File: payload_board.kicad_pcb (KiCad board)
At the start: 4 copper layers, 100 x 100 mm, 100 parts, among them IC1 RP2040_QFN56, IC2 AZ1117CH-3.3TRG1, J1 Cam_PicoLock, J12 5025700893, J12 FC Breakout, J15 SWC, J2 Cam_Conn, J3 Antenna_Conn, J4 usb jumper, J5 Display_Conn, J6 Breakout, J7 Molex_Micro_USB, J8 FC to EPS Connector, Q1 Q_PMOS_GSD, SW1 KMR2, SW2 KMR2, T13V TESTPOINTROUND1.5MMNO, T1V2 TESTPOINTROUND1.5MMNO, T3V3 TESTPOINTROUND1.5MMNO, U1 W25Q128JVPIQ TR, U2 MAX706RESA, U3 INA180A1, U4 INA180A1, U5 FAN5331SX, Y1 ABLS-12.000MHZ-B2-T

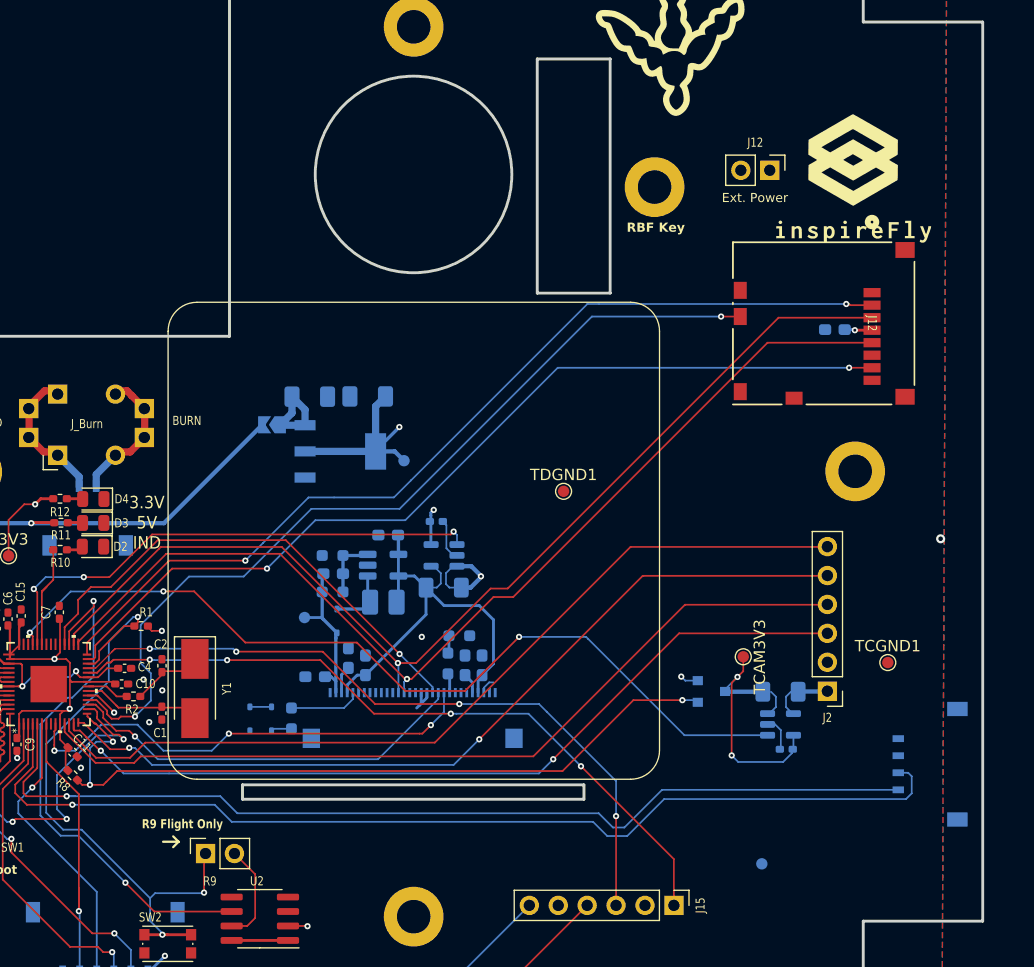
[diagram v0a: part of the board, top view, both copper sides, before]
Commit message: Moved some line appart
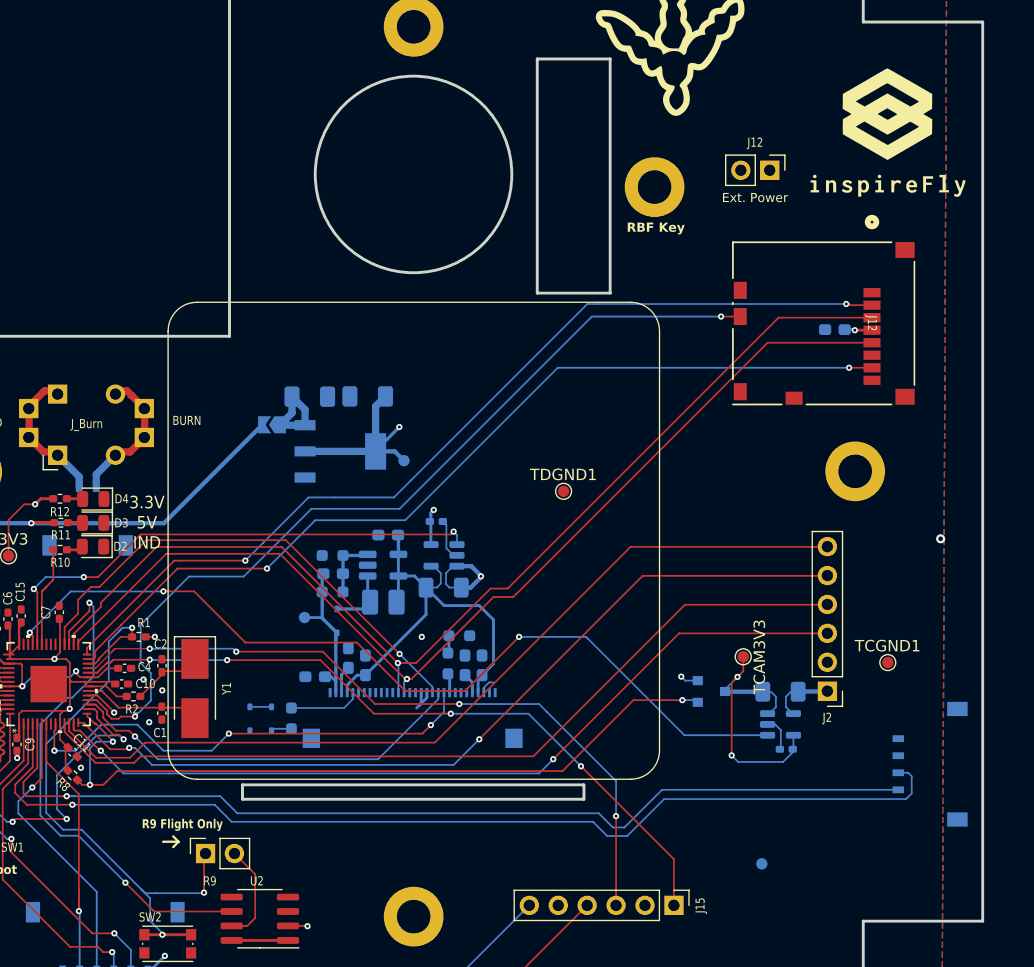
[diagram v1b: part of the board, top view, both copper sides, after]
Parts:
- moved G*** 5.04 mm to (104.6, 33.0)
- moved R1 0.97 mm to (38.8, 77.5)
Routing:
- net /~{RESET}: track 56.1 -> 55.1 mm
- net +3.3V: track 97.7 -> 97.0 mm

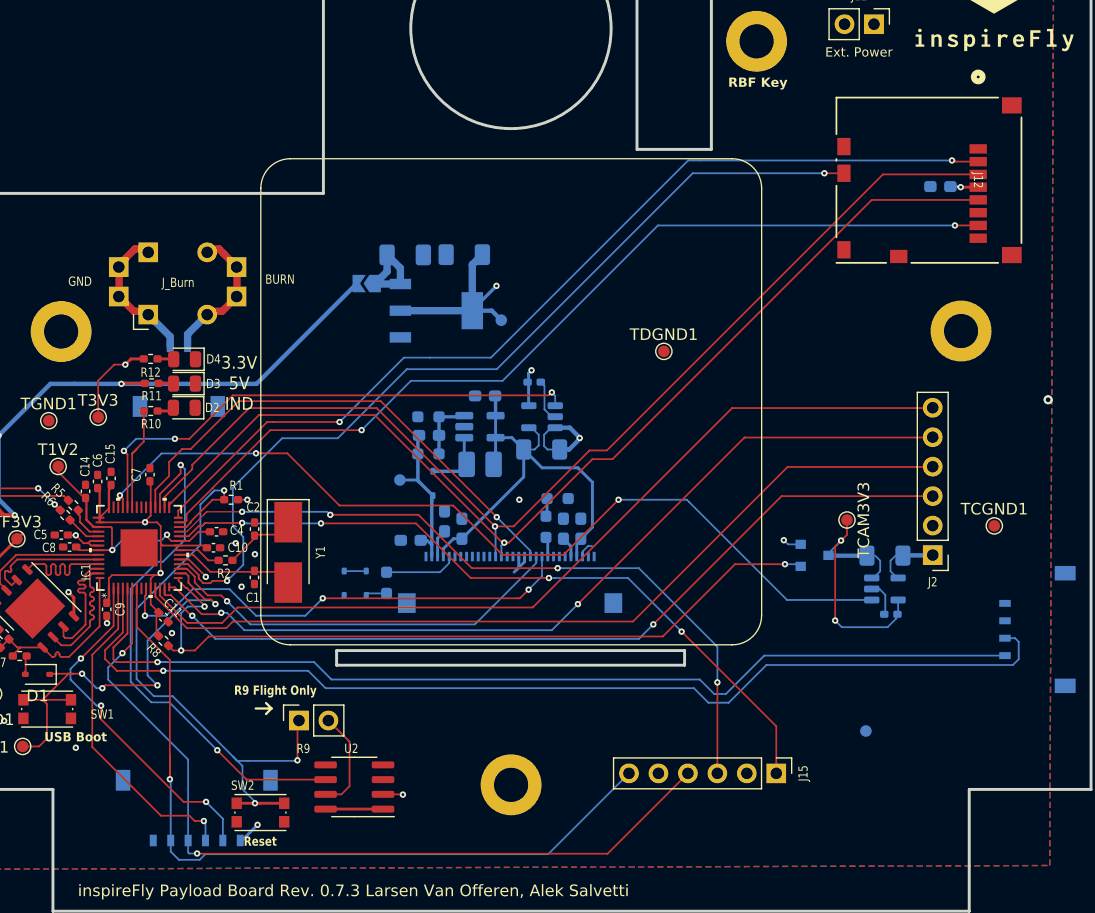
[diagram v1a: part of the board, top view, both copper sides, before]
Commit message: Fixed RP2040 connections and changed sd card
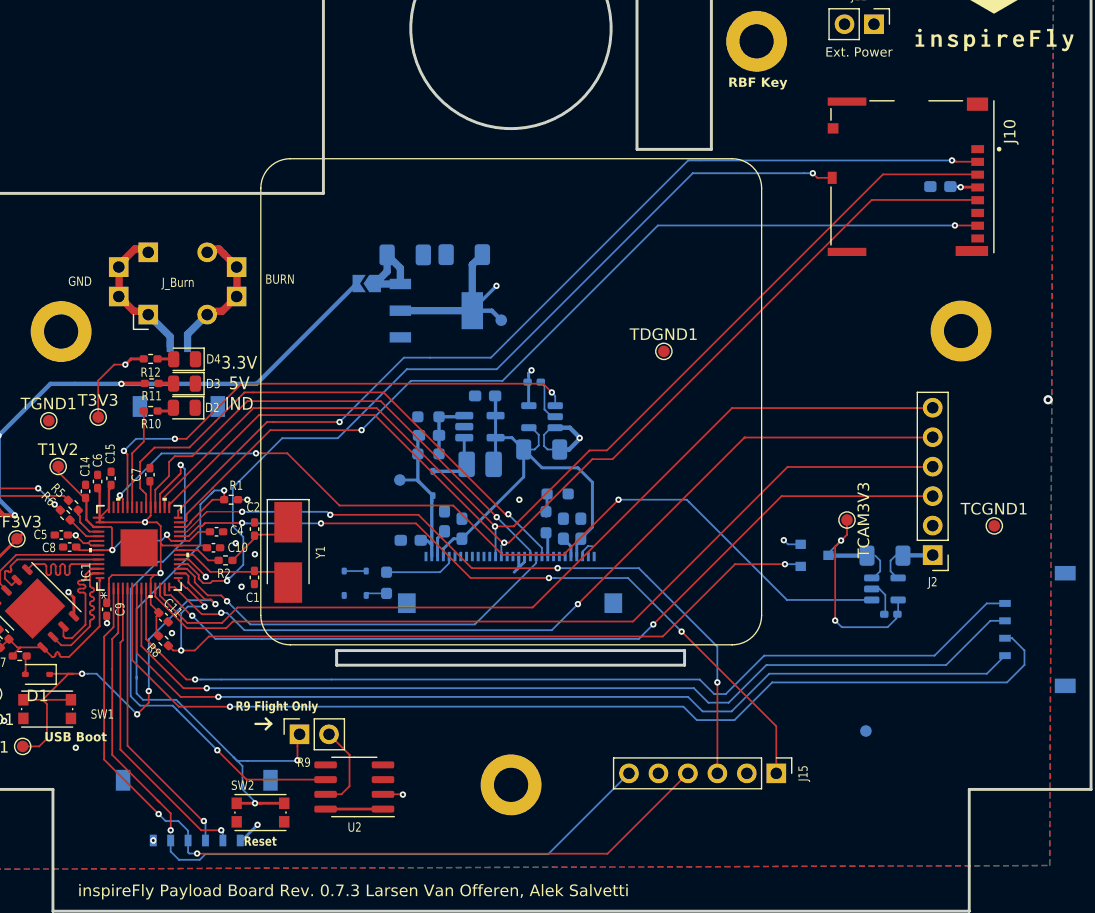
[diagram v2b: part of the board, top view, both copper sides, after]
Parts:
- removed the J12 at (99.0, 50.0)
- added J10: 503398-1892, PayloadBoard:MOLEX_503398-1892, F.Cu at (97.6, 49.7)
- moved R9 1.19 mm to (44.8, 97.7)
- moved R15 0.40 mm to (66.0, 79.4)
- moved R16 0.40 mm to (67.0, 77.0)
- turned C18 to 0 degrees
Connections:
- C18 pad 1: +3.3V -> GND
- C18 pad 2: GND -> +3.3V
- IC1 pad 2: Break_SDA -> UART1_TX
- IC1 pad 3: Break_SCL -> UART1_RX
- IC1 pad 34: unconnected-(IC1-GPIO22-Pad34) -> Disp_RST
- IC1 pad 4: I2C1_SDA -> Break_SDA
- IC1 pad 5: I2C1_SCL -> Break_SCL
- IC1 pad 6: UART1_TX -> I2C1_SDA
- IC1 pad 7: UART1_RX -> I2C1_SCL
- IC1 pad 8: unconnected-(IC1-GPIO6-Pad8) -> BURN_A
- IC1 pad 9: Disp_RST -> BURN_B
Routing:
- net BURN_A: track 0.00 -> 84.4 mm, vias 0 -> 1
- net BURN_B: track 0.00 -> 83.6 mm, vias 0 -> 1
- net Disp_RST: track 41.7 -> 47.6 mm, vias 3 -> 1
- net Break_SCL: track 28.7 -> 24.7 mm
- net Break_SDA: track 30.2 -> 26.6 mm, vias 3 -> 1
- net I2C1_SCL: track 86.7 -> 84.6 mm
- net /USBBOOT: track 39.8 -> 41.5 mm
- net UART1_RX: track 68.9 -> 67.3 mm
- net Net-(U2-~{RESET}): track 8.77 -> 7.56 mm
- net SD_IND: track 78.0 -> 77.2 mm
- net I2C1_SDA: track 91.5 -> 90.7 mm
- net WDT_WDI: track 45.8 -> 46.6 mm
- net ADC0: track 45.3 -> 45.9 mm
- net /QSPI_DATA[2]: track 11.0 -> 11.6 mm
- net Net-(IC1-GPIO25): track 9.40 -> 8.81 mm
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
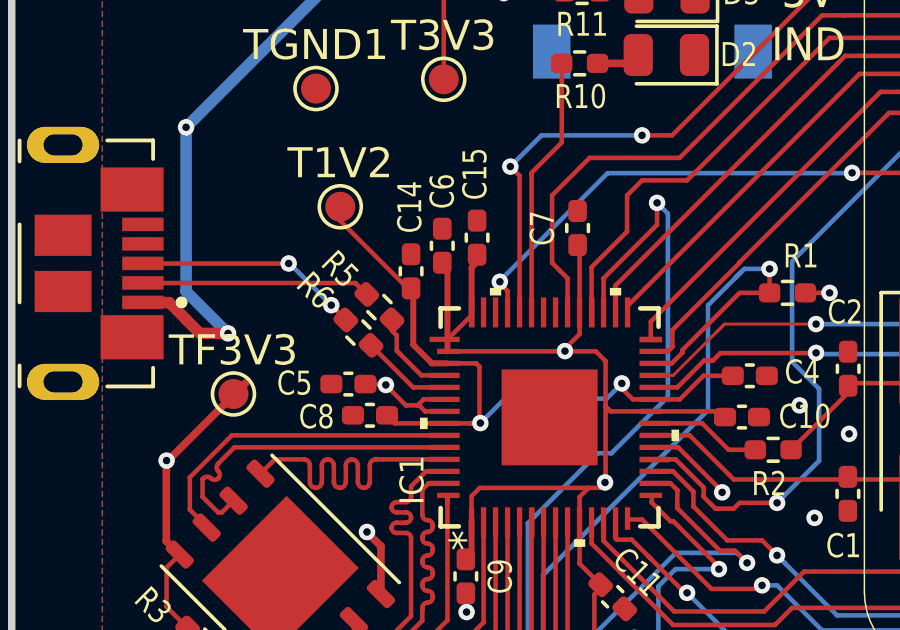
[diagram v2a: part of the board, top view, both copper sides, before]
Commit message: changed footprint for sd card and fixed not gnd planes
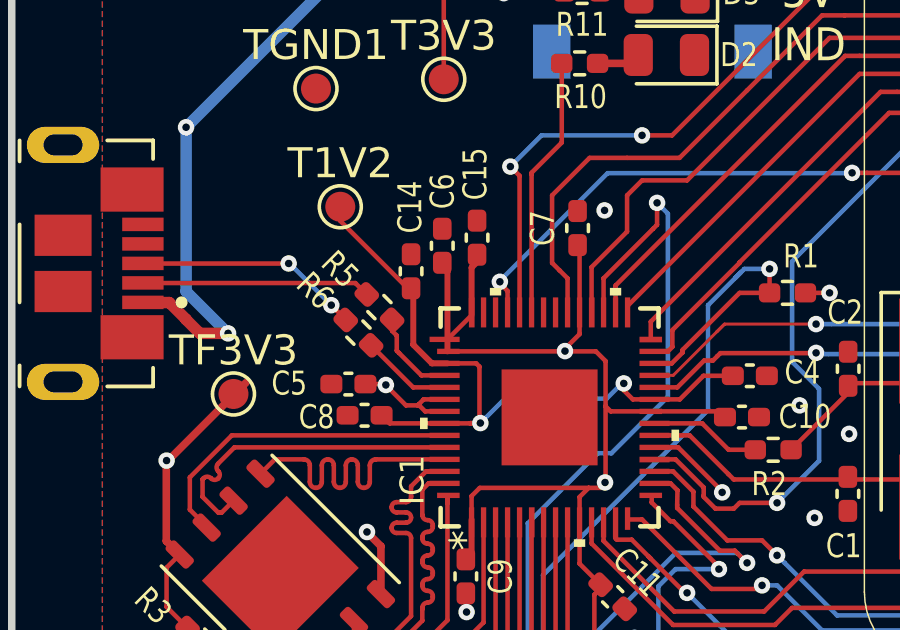
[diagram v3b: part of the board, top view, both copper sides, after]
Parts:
- moved C5 0.18 mm to (24.8, 81.6)
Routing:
- net GND: vias 12 -> 13

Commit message: Fixed some errors and added manufactering file
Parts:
- moved TDGND1 3.46 mm to (73.5, 62.5)
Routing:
- net UART1_RX: track 67.3 -> 67.9 mm
- net VBUS: vias 3 -> 2
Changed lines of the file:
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@@
 		(allow_soldermask_bridges_in_footprints no)
 		(pcbplotparams
-			(layerselection 0x00010fc_ffffffff)
+			(layerselection 0x00010f0_ffffffff)
 			(plot_on_all_layers_selection 0x0000000_00000000)
 			(disableapertmacros no)
@@
 			(plotinvisibletext no)
 			(sketchpadsonfab no)
-			(subtractmaskfromsilk no)
+			(subtractmaskfromsilk yes)
 			(outputformat 1)
 			(mirror no)
 			(drillshape 0)
 			(scaleselection 1)
-			(outputdirectory "Manufacturing/payload_board_rev072_gbr")
+			(outputdirectory "Manufacturing/payload_board_rev073_gbr")
 		)
 	)
@@
 	(footprint "TestPoint:TestPoint_Pad_D1.0mm"
 		(layer "F.Cu")
-		(at 76.16 64.71)
+		(at 73.5 62.5)
 		(descr "SMD pad as test Point, diameter 1.0mm")
 		(tags "test point SMD pad")
@@
 		(tags "capacitor handsolder")
 		(property "Reference" "C18"
-			(at 0 1.43 360)
+			(at 0 1.43 0)
 			(layer "B.SilkS")
 			(effects
@@
 		)
 		(property "Value" "10uF"
-			(at 0 -1.43 360)
+			(at 0 -1.43 0)
 			(layer "B.Fab")
 			(effects
@@
 		)
 		(fp_text user "${REFERENCE}"
-			(at 0 0 360)
+			(at 0 0 0)
 			(layer "B.Fab")
 			(effects
@@
 	)
 	(segment
-		(start 33.6567 85.7267)
+		(start 33.116401 85.682301)
 		(end 33.1608 85.7267)
 		(width 0.1524)
@@
 	)
 	(segment
+		(start 33.116401 85.1486)
+		(end 33.116401 85.682301)
+		(width 0.1524)
+		(layer "F.Cu")
+		(net 14)
+	)
+	(segment
 		(start 86.31 77.19)
 		(end 99.34 77.19)
@@
 	(segment
 		(start 33.1608 85.7267)
-		(end 33.116401 85.682301)
+		(end 33.6567 85.7267)
 		(width 0.1524)
 		(layer "F.Cu")
@@
 	)
 	(segment
-		(start 34.279426 86.349426)
+		(start 33.6567 85.7267)
 		(end 34.215 86.285)
 		(width 0.1524)
@@
 	(segment
 		(start 34.215 86.285)
-		(end 33.6567 85.7267)
-		(width 0.1524)
-		(layer "F.Cu")
-		(net 14)
-	)
-	(segment
-		(start 34.215 86.285)
 		(end 35.43 87.5)
 		(width 0.1524)
@@
 	)
 	(segment
-		(start 33.116401 85.682301)
-		(end 33.116401 85.0536)
-		(width 0.1524)
-		(layer "F.Cu")
-		(net 14)
-	)
-	(segment
 		(start 75.25 88.25)
 		(end 86.31 77.19)
@@
 		(net 14)
 	)
-	(segment
-		(start 34.279426 86.350574)
-		(end 34.279426 86.349426)
-		(width 0.1524)
-		(layer "F.Cu")
-		(net 14)
-	)
 	(via
 		(at 35.5 87.5)
@@
 	)
 	(segment
-		(start 31.7706 89.5206)
-		(end 31.6456 89.6456)
-		(width 0.1524)
-		(layer "B.Cu")
-		(net 17)
-	)
-	(segment
 		(start 26.5 92.5)
 		(end 26 92.5)
@@
 	)
 	(segment
-		(start 30.6983 92.9483)
-		(end 30.6983 92.75)
-		(width 0.1524)
-		(layer "B.Cu")
-		(net 22)
-	)
-	(segment
 		(start 36.1983 81.4037)
 		(end 36.1983 77.9117)
@@
 	)
 	(segment
-		(start 70 74)
-		(end 71.734934 74)
-		(width 0.1524)
-		(layer "F.Cu")
-		(net 25)
-	)
-	(segment
 		(start 33.5164 78.1514)
 		(end 33.5164 77.9336)
@@
 	)
 	(segment
-		(start 62.8 81.2)
-		(end 70 74)
-		(width 0.1524)
-		(layer "F.Cu")
-		(net 25)
-	)
-	(segment
 		(start 62.4 81.2)
 		(end 62.8 81.2)
@@
 	)
 	(segment
-		(start 94.081635 51.653299)
-		(end 103.262151 51.653299)
+		(start 33.5164 77.9336)
+		(end 41.25 70.2)
 		(width 0.1524)
 		(layer "F.Cu")
@@
 	)
 	(segment
-		(start 71.734934 74)
-		(end 94.081635 51.653299)
+		(start 92.346701 51.653299)
+		(end 103.262151 51.653299)
 		(width 0.1524)
 		(layer "F.Cu")
@@
 	)
 	(segment
-		(start 33.5164 77.9336)
-		(end 41.25 70.2)
+		(start 62.8 81.2)
+		(end 92.346701 51.653299)
 		(width 0.1524)
 		(layer "F.Cu")
@@
 	)
 	(segment
-		(start 40.77 69.6)
-		(end 41.25 69.6)
-		(width 0.1524)
-		(layer "F.Cu")
-		(net 26)
-	)
-	(segment
-		(start 33.116401 78.2464)
-		(end 33.116401 77.253599)
-		(width 0.1524)
-		(layer "F.Cu")
-		(net 26)
-	)
-	(segment
-		(start 41.25 69.6)
-		(end 51.4 69.6)
+		(start 63.2 79.8)
+		(end 93.546699 49.453301)
 		(width 0.1524)
 		(layer "F.Cu")
@@
 	)
 	(segment
-		(start 51.4 69.6)
-		(end 61.6 79.8)
+		(start 40.77 69.6)
+		(end 41.25 69.6)
 		(width 0.1524)
 		(layer "F.Cu")
@@
 	)
 	(segment
-		(start 69.75 73.25)
-		(end 71.25 73.25)
+		(start 61.6 79.8)
+		(end 63.2 79.8)
 		(width 0.1524)
 		(layer "F.Cu")
@@
 	)
 	(segment
-		(start 71.25 73.25)
-		(end 95.046699 49.453301)
+		(start 33.116401 78.2464)
+		(end 33.116401 77.253599)
 		(width 0.1524)
 		(layer "F.Cu")
@@
 	)
 	(segment
-		(start 33.116401 77.253599)
-		(end 40.77 69.6)
+		(start 41.25 69.6)
+		(end 51.4 69.6)
 		(width 0.1524)
 		(layer "F.Cu")
@@
 	)
 	(segment
-		(start 61.6 79.8)
-		(end 63.2 79.8)
+		(start 93.546699 49.453301)
+		(end 103.262151 49.453301)
 		(width 0.1524)
 		(layer "F.Cu")
@@
 	)
 	(segment
-		(start 63.2 79.8)
-		(end 69.75 73.25)
+		(start 51.4 69.6)
+		(end 61.6 79.8)
 		(width 0.1524)
 		(layer "F.Cu")
@@
 	)
 	(segment
-		(start 95.046699 49.453301)
-		(end 103.262151 49.453301)
+		(start 33.116401 77.253599)
+		(end 40.77 69.6)
 		(width 0.1524)
 		(layer "F.Cu")
@@
 	)
 	(via
-		(at 18.8 71.98)
-		(size 0.55)
-		(drill 0.25)
-		(layers "F.Cu" "B.Cu")
-		(net 46)
-	)
-	(via
 		(at 29.39 67.51)
 		(size 0.55)
@@
 	)
 	(segment
-		(start 32.5 103.4)
-		(end 32.7 103.6)
-		(width 0.1524)
-		(layer "F.Cu")
-		(net 54)
-	)
-	(segment
 		(start 29.116401 85.1486)
 		(end 29.116401 88.983599)
@@
 		(width 0.1524)
 		(layer "B.Cu")
+		(net 54)
+	)
+	(segment
+		(start 33.640348 106.880001)
+		(end 33.640348 106)
+		(width 0.1524)
+		(layer "B.Cu")

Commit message: Update BOM and part identifiers on PCB
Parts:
- R13: value 10k -> 0.065
- U3, U4: value INA180A1 -> INA180A3
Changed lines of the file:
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@@
 			)
 		)
-		(property "Value" "10k"
+		(property "Value" "0.065"
 			(at 0 -1.82 0)
 			(layer "B.Fab")
@@
 			)
 		)
-		(property "Value" "INA180A1"
+		(property "Value" "INA180A3"
 			(at 0 -2.4 0)
 			(layer "B.Fab")
@@
 			)
 		)
-		(property "Value" "INA180A1"
+		(property "Value" "INA180A3"
 			(at 0 -2.4 0)
 			(layer "B.Fab")

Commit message: Updated footprints
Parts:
- moved TCGND1 9.06 mm to (101.5, 88.2)
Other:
- board text added: "3V3"
- board text added: "CS"
- board text added: "GND"
- board text added: "MISO"
- board text added: "MOSI"
- board text added: "SCK"
- board text added: "SWCLK"
- board text added: "SWDIO"
- board text added: "UART_RX"
- board text added: "UART_TX"
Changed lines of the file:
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@@
 		(tags "Through hole pin header THT 1x02 2.54mm single row")
 		(property "Reference" "J12"
-			(at -2.4384 1.27 0)
+			(at -0.1 -2.725 0)
 			(layer "F.SilkS")
 			(effects
@@
 		)
 		(property "Value" "FC Breakout"
-			(at -2.3 0.54 0)
+			(at -2.3 -2.325 0)
 			(layer "F.Fab")
 			(effects
@@
 	(footprint "TestPoint:TestPoint_Pad_D1.0mm"
 		(layer "F.Cu")
-		(at 104.648 79.756)
+		(at 101.5 88.25)
 		(descr "SMD pad as test Point, diameter 1.0mm")
 		(tags "test point SMD pad")
@@
 		)
 	)
+	(gr_text "SWDIO"
+		(at 80.25 102.9 270)
+		(layer "F.SilkS")
+		(effects
+			(font
+				(size 0.8 0.8)
+				(thickness 0.125)
+				(bold yes)
+			)
+			(justify left bottom)
+		)
+	)
 	(gr_text "3.3V\n5V\nIND"
 		(at 39.55 69.88 0)
@@
 		)
 	)
+	(gr_text "CS"
+		(at 101.5 70 0)
+		(layer "F.SilkS")
+		(effects
+			(font
+				(size 0.8 0.8)
+				(thickness 0.125)
+				(bold yes)
+			)
+			(justify left bottom)
+		)
+	)
+	(gr_text "UART_TX"
+		(at 77.75 102.9 270)
+		(layer "F.SilkS")
+		(effects
+			(font
+				(size 0.8 0.8)
+				(thickness 0.125)
+				(bold yes)
+			)
+			(justify left bottom)
+		)
+	)
+	(gr_text "SCK"
+		(at 101.5 77.5 0)
+		(layer "F.SilkS")
+		(effects
+			(font
+				(size 0.8 0.8)
+				(thickness 0.125)
+				(bold yes)
+			)
+			(justify left bottom)
+		)
+	)
 	(gr_text "inspireFly Payload Board Rev. 0.7.3 Larsen Van Offeren, Alek Salvetti"
 		(at 25.63 111.8 0)
@@
 		)
 	)
+	(gr_text "3V3"
+		(at 101.75 82.75 0)
+		(layer "F.SilkS")
+		(effects
+			(font
+				(size 0.8 0.8)
+				(thickness 0.125)
+				(bold yes)
+			)
+			(justify left bottom)
+		)
+	)
 	(gr_text "Ext. Power"
 		(at 90.06 39.39 0)
@@
 		)
 	)
+	(gr_text "GND"
+		(at 94.75 34.75 90)
+		(layer "F.SilkS")
+		(effects
+			(font
+				(size 0.8 0.8)
+				(thickness 0.125)
+				(bold yes)
+			)
+			(justify left bottom)
+		)
+	)
+	(gr_text "MOSI"
+		(at 101.5 72.5 0)
+		(layer "F.SilkS")
+		(effects
+			(font
+				(size 0.8 0.8)
+				(thickness 0.125)
+				(bold yes)
+			)
+			(justify left bottom)
+		)
+	)
+	(gr_text "GND"
+		(at 75.2 102.9 -90)
+		(layer "F.SilkS")
+		(effects
+			(font
+				(size 0.8 0.8)
+				(thickness 0.125)
+				(bold yes)
+			)
+			(justify left bottom)
+		)
+	)
 	(gr_text "RBF Key"
 		(at 81.7 42 0)
@@
 		)
 	)
+	(gr_text "MISO"
+		(at 101.5 75 0)
+		(layer "F.SilkS")
+		(effects
+			(font
+				(size 0.8 0.8)
+				(thickness 0.125)
+				(bold yes)
+			)
+			(justify left bottom)
+		)
+	)
+	(gr_text "3V3"
+		(at 92.25 34.75 90)
+		(layer "F.SilkS")
+		(effects
+			(font
+				(size 0.8 0.8)
+				(thickness 0.125)
+				(bold yes)
+			)
+			(justify left bottom)
+		)
+	)
+	(gr_text "GND"
+		(at 101.5 80.25 0)
+		(layer "F.SilkS")
+		(effects
+			(font
+				(size 0.8 0.8)
+				(thickness 0.125)
+				(bold yes)
+			)
+			(justify left bottom)
+		)
+	)
+	(gr_text "SWCLK"
+		(at 85.4 102.9 270)
+		(layer "F.SilkS")
+		(effects
+			(font
+				(size 0.8 0.8)
+				(thickness 0.125)
+				(bold yes)
+			)
+			(justify left bottom)
+		)
+	)
 	(gr_text "JLCJLCJLCJLC"
 		(at 53.848 15.494 0)
@@
 				(bold yes)
 			)
+			(justify left bottom)
+		)
+	)
+	(gr_text "UART_RX"
+		(at 72.6 102.9 -90)
+		(layer "F.SilkS")
+		(effects
+			(font
+				(size 0.8 0.8)
+				(thickness 0.125)
+				(bold yes)
+			)
+			(justify left bottom)
+		)
+	)
+	(gr_text "GND"
+		(at 82.8 102.9 -90)
+		(layer "F.SilkS")
+		(effects
+			(font
+				(size 0.8 0.8)
+				(thickness 0.125)
+				(bold yes)
+			)
